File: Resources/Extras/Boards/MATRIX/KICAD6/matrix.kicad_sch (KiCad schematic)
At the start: 20 parts, among them J1 Conn_01x24, J2 Conn_01x24, J3 Conn_01x24, J4 Conn_01x24, U1 Teensy4.1

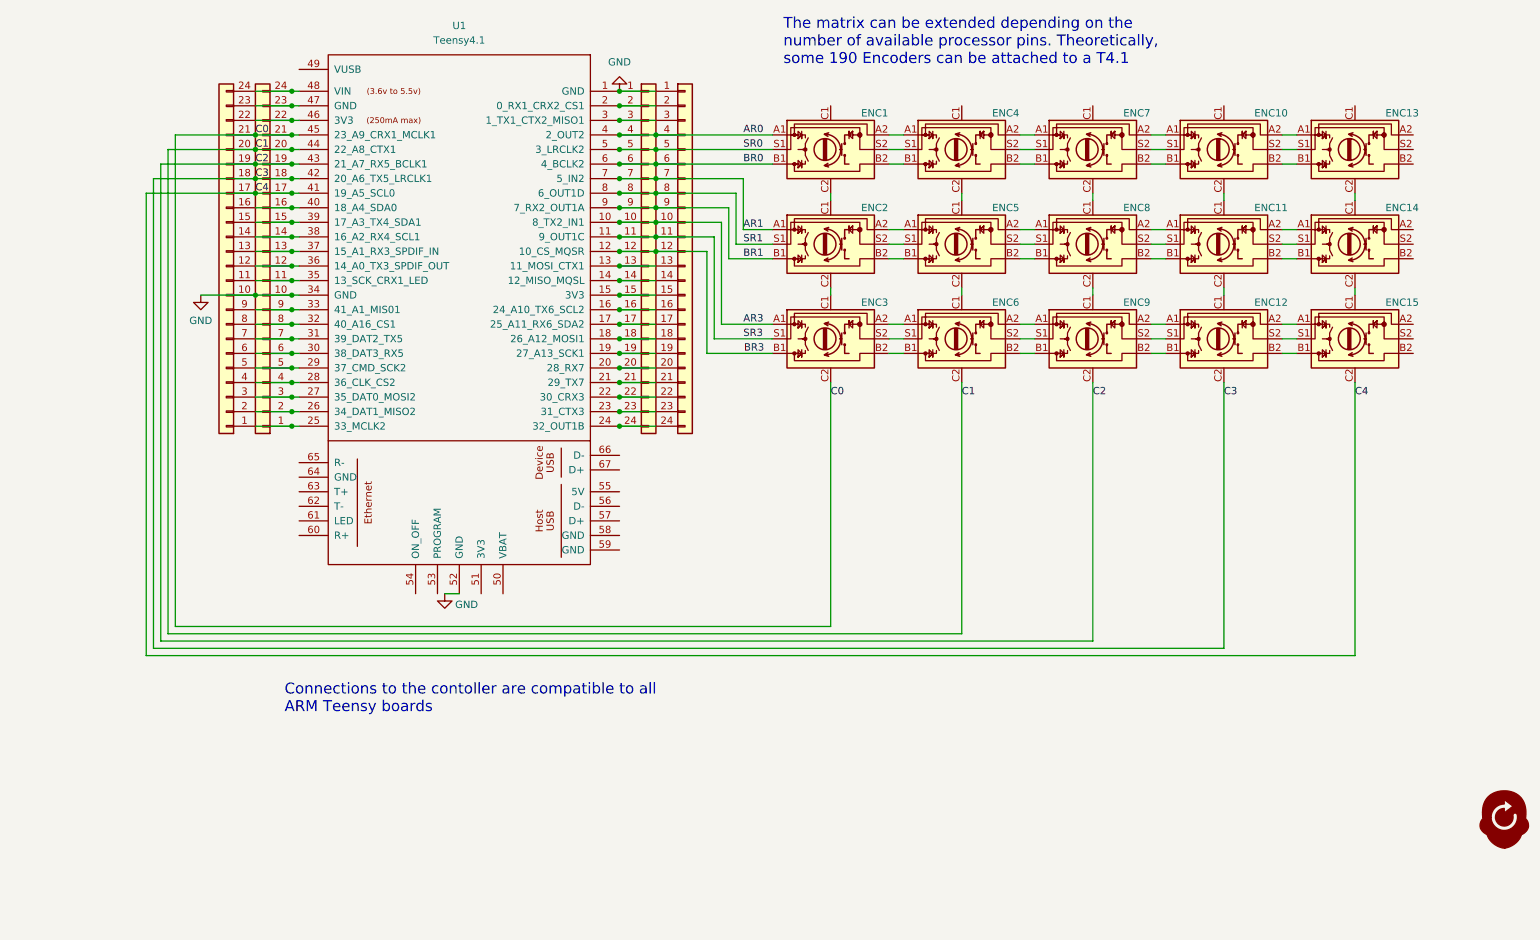
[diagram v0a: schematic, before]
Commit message: Fixed errors in matrix test board
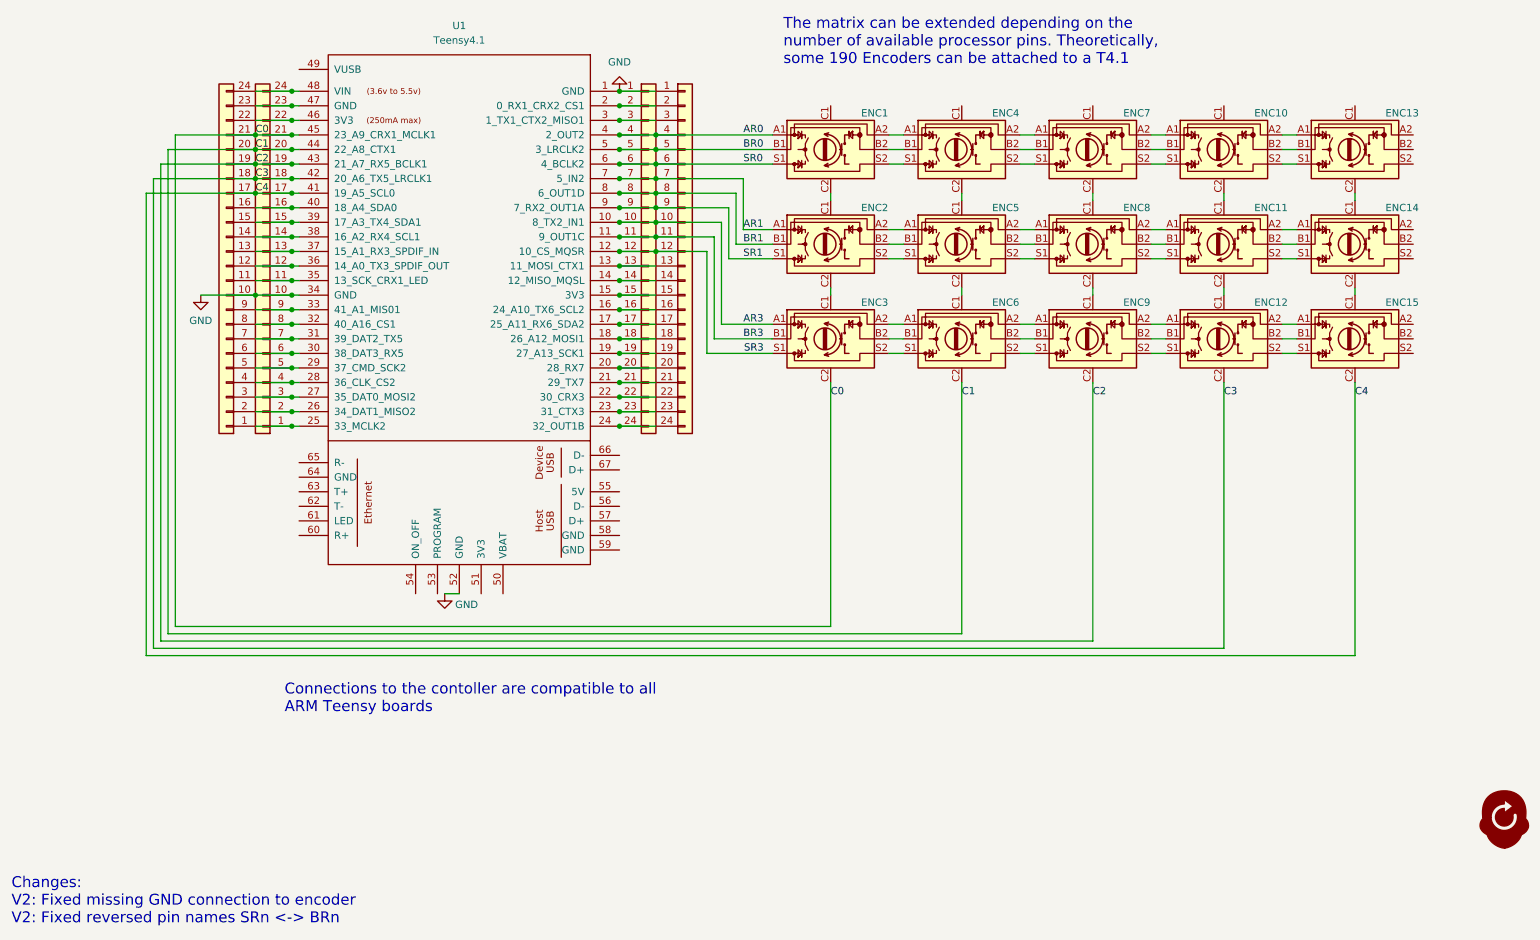
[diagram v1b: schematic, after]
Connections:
- net BR0: now also J3.5 (Pin_5), J4.5 (Pin_5), U1.5 (3_LRCLK2); no longer J3.6 (Pin_6), J4.6 (Pin_6), U1.6 (4_BCLK2)
- net BR1: now also J3.8 (Pin_8), J4.8 (Pin_8), U1.8 (6_OUT1D); no longer J3.9 (Pin_9), J4.9 (Pin_9), U1.9 (7_RX2_OUT1A)
- net BR3: now also J3.11 (Pin_11), J4.11 (Pin_11), U1.11 (9_OUT1C); no longer J3.12 (Pin_12), J4.12 (Pin_12), U1.12 (10_CS_MQSR)
- net SR0: now also J3.6 (Pin_6), J4.6 (Pin_6), U1.6 (4_BCLK2); no longer J3.5 (Pin_5), J4.5 (Pin_5), U1.5 (3_LRCLK2)
- net SR1: now also J3.9 (Pin_9), J4.9 (Pin_9), U1.9 (7_RX2_OUT1A); no longer J3.8 (Pin_8), J4.8 (Pin_8), U1.8 (6_OUT1D)
- net SR3: now also J3.12 (Pin_12), J4.12 (Pin_12), U1.12 (10_CS_MQSR); no longer J3.11 (Pin_11), J4.11 (Pin_11), U1.11 (9_OUT1C)
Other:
- note added: "Changes: V2: Fixed missing GND connection to encoder V2: Fixed reversed pin names SRn <-> BRn"
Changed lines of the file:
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@@
     (title "Encoder Matrix Proto Board")
     (date "2022-05-23")
-    (rev "1")
+    (rev "2")
     (company "lunOptics")
   )
@@
   (wire (pts (xy 128.905 57.785) (xy 149.225 57.785))
     (stroke (width 0) (type default) (color 0 0 0 0))
+  )
+  (text "Changes: \nV2: Fixed missing GND connection to encoder\nV2: Fixed reversed pin names SRn <-> BRn"
+    (at 16.51 193.04 0)
+    (effects (font (size 1.905 1.905)) (justify left bottom))
   )
   (text "Connections to the contoller are compatible to all \nARM Teensy boards"
@@
     (effects (font (size 1.27 1.27)) (justify left bottom))
   )
-  (label "SR3" (at 144.145 90.805 0)
-    (effects (font (size 1.27 1.27)) (justify left bottom))
-  )
-  (label "SR1" (at 144.145 74.295 0)
+  (label "BR3" (at 144.145 90.805 0)
+    (effects (font (size 1.27 1.27)) (justify left bottom))
+  )
+  (label "BR1" (at 144.145 74.295 0)
     (effects (font (size 1.27 1.27)) (justify left bottom))
   )
@@
     (effects (font (size 1.27 1.27)) (justify left bottom))
   )
-  (label "BR0" (at 144.145 60.325 0)
+  (label "SR0" (at 144.145 60.325 0)
     (effects (font (size 1.27 1.27)) (justify left bottom))
   )
@@
     (effects (font (size 1.27 1.27)) (justify left bottom))
   )
-  (label "BR1" (at 144.145 76.835 0)
-    (effects (font (size 1.27 1.27)) (justify left bottom))
-  )
-  (label "BR3" (at 144.272 93.345 0)
+  (label "SR1" (at 144.145 76.835 0)
+    (effects (font (size 1.27 1.27)) (justify left bottom))
+  )
+  (label "SR3" (at 144.272 93.345 0)
     (effects (font (size 1.27 1.27)) (justify left bottom))
   )
@@
     (effects (font (size 1.27 1.27)) (justify left bottom))
   )
-  (label "SR0" (at 144.145 57.785 0)
-    (effects (font (size 1.27 1.27)) (justify left bottom))
-  )
+  (label "BR0" (at 144.145 57.785 0)
+    (effects (font (size 1.27 1.27)) (justify left bottom))
+  )
